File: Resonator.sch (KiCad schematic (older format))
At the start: 25 parts, among them SW1 SW_Push, U1 PCM3060, U5 STM32H750VBTx, Y1 25MHz

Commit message: Chanced regulators and oscillator work.
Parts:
- added R2: 10k, Resistor_SMD:R_0603_1608Metric, symbol Device:R
- added R3: 470, Resistor_SMD:R_0603_1608Metric, symbol Device:R
- C11: renamed from C43; footprint Capacitor_SMD:C_0603_1608Metric -> Capacitor_SMD:C_0402_1005Metric
- C12: renamed from C44; footprint Capacitor_SMD:C_0603_1608Metric -> Capacitor_SMD:C_0402_1005Metric
- C13: renamed from C45; footprint Capacitor_SMD:C_0603_1608Metric -> Capacitor_SMD:C_0402_1005Metric
- C15: renamed from C47; footprint Capacitor_SMD:C_0603_1608Metric -> Capacitor_SMD:C_0402_1005Metric
- C16: renamed from C1; footprint Capacitor_SMD:C_0603_1608Metric -> Capacitor_SMD:C_0402_1005Metric
- C17: renamed from C2; footprint Capacitor_SMD:C_0603_1608Metric -> Capacitor_SMD:C_0402_1005Metric
- C18: renamed from C3; footprint Capacitor_SMD:C_0603_1608Metric -> Capacitor_SMD:C_0402_1005Metric
- C2: renamed from C34; footprint Capacitor_SMD:C_0603_1608Metric -> Capacitor_SMD:C_0402_1005Metric
- C3: renamed from C35; footprint Capacitor_SMD:C_0603_1608Metric -> Capacitor_SMD:C_0402_1005Metric
- C4: renamed from C36; footprint Capacitor_SMD:C_0603_1608Metric -> Capacitor_SMD:C_0402_1005Metric
- C5: renamed from C37; footprint Capacitor_SMD:C_0603_1608Metric -> Capacitor_SMD:C_0402_1005Metric
- C6: renamed from C41; value 3p9 -> 22p; footprint Capacitor_SMD:C_0603_1608Metric -> Capacitor_SMD:C_0402_1005Metric
- C7: renamed from C42; value 3p9 -> 22p; footprint Capacitor_SMD:C_0603_1608Metric -> Capacitor_SMD:C_0402_1005Metric
- C9: renamed from C39; footprint Capacitor_SMD:C_0603_1608Metric -> Capacitor_SMD:C_0402_1005Metric
- R1: renamed from R23; value 10k -> UNPOPULATED
- SW1: footprint (none) -> Button_Switch_THT:SW_PUSH_6mm
- Y1: value 25MHz -> ABM8G-25.000MHZ-18-D2Y-T; footprint (none) -> Crystal:Crystal_SMD_Abracon_ABM8G-4Pin_3.2x2.5mm
- renumbered C33 to C1, C40 to C10, C46 to C14, C4 to C19, C38 to C8, R1 to R4, U5 to U1, U1 to U2
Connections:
- net +3V3: now also R1.2
- net GND: now also R2.1
- net at C7.1, Y1.3: now also R3.2; no longer U1.13 (PH1)
- net at R1.1, U1.94 (BOOT0): now also R2.2
- new net: R3.1, U1.13 (PH1)
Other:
- moved on the sheet: C6, C7, R1, Y1

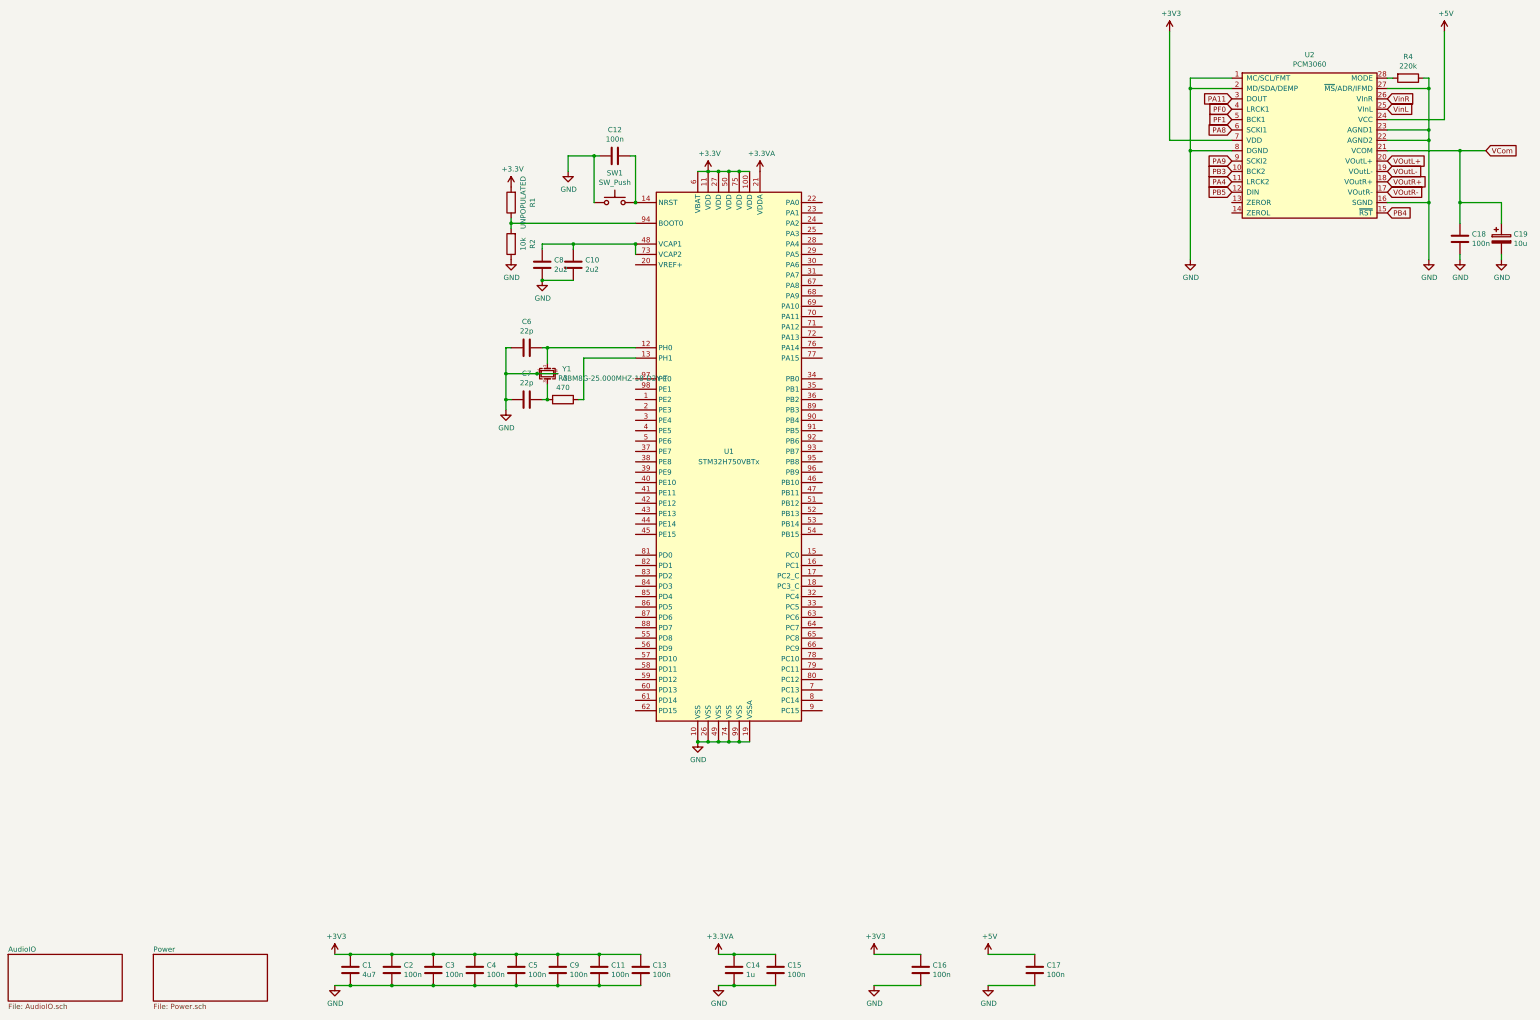
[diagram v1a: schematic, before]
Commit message: Added UI components.
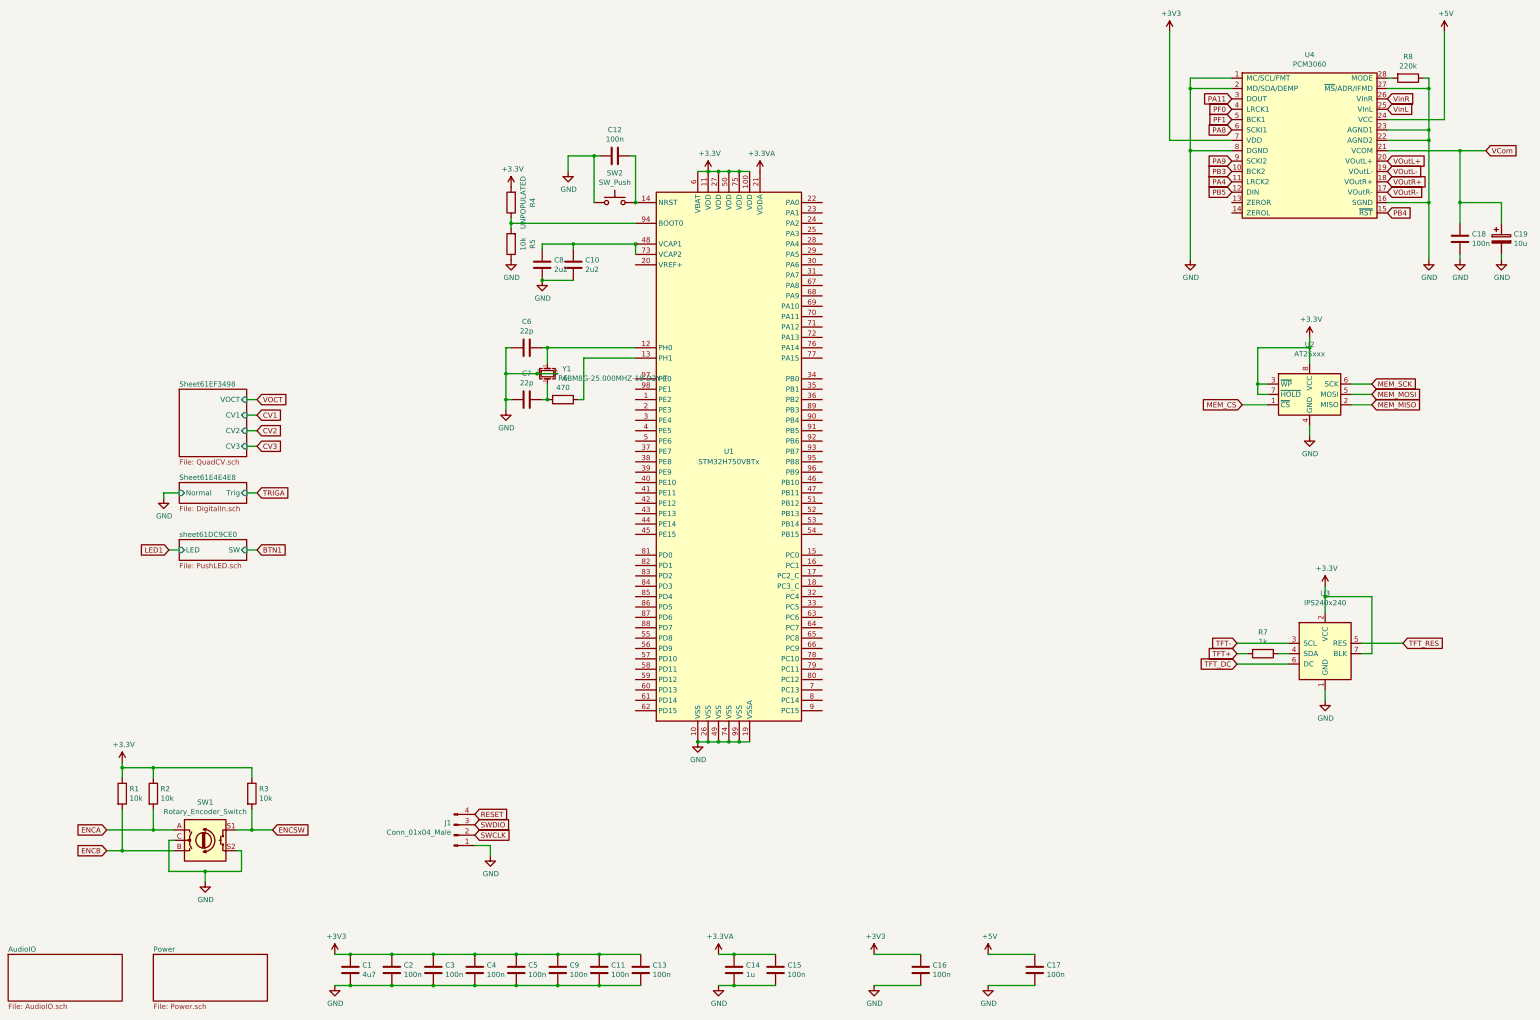
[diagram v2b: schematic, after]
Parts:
- added J1: Conn_01x04_Male, Connector_PinHeader_2.54mm:PinHeader_1x04_P2.54mm_Vertical, symbol Connector:Conn_01x04_Male
- added R1, R2, R3: 10k, Resistor_SMD:R_0603_1608Metric, symbol Device:R
- added R7: 1k, Resistor_SMD:R_0603_1608Metric, symbol Device:R
- added SW1: Rotary_Encoder_Switch, Rotary_Encoder:RotaryEncoder_Alps_EC11E-Switch_Vertical_H20mm, symbol Device:Rotary_Encoder_Switch
- added U2: AT25xxx, Package_SO:TSSOP-8_4.4x3mm_P0.65mm, symbol Memory_EEPROM:AT25xxx
- added U3: IPS240x240, symbol IPS240x240:IPS240x240
- renumbered R1 to R4, R2 to R5, R3 to R6, R4 to R8, SW1 to SW2, U2 to U4
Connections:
- net +3V3: now also R1.1, R2.1, R3.1, U2.3 (~WP), U2.7 (~HOLD), U2.8 (VCC), U3.2 (VCC), U3.7 (BLK)
- net GND: now also J1.1 (Pin_1), SW1.C, SW1.S2, U2.4 (GND), U3.1 (GND)
- new net: R7.1, U3.4 (SDA)
- new net ENCA: R2.2, SW1.A
- new net ENCB: R1.2, SW1.B
- new net ENCSW: R3.2, SW1.S1
- new net MEM_CS: U2.1 (~CS)
- new net MEM_MISO: U2.2 (MISO)
- new net MEM_MOSI: U2.5 (MOSI)
- new net MEM_SCK: U2.6 (SCK)
- new net RESET: J1.4 (Pin_4)
- new net SWCLK: J1.2 (Pin_2)
- new net SWDIO: J1.3 (Pin_3)
- new net TFT+: R7.2
- new net TFT-: U3.3 (SCL)
- new net TFT_DC: U3.6 (DC)
- new net TFT_RES: U3.5 (RES)

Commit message: Moved codec to audio module.
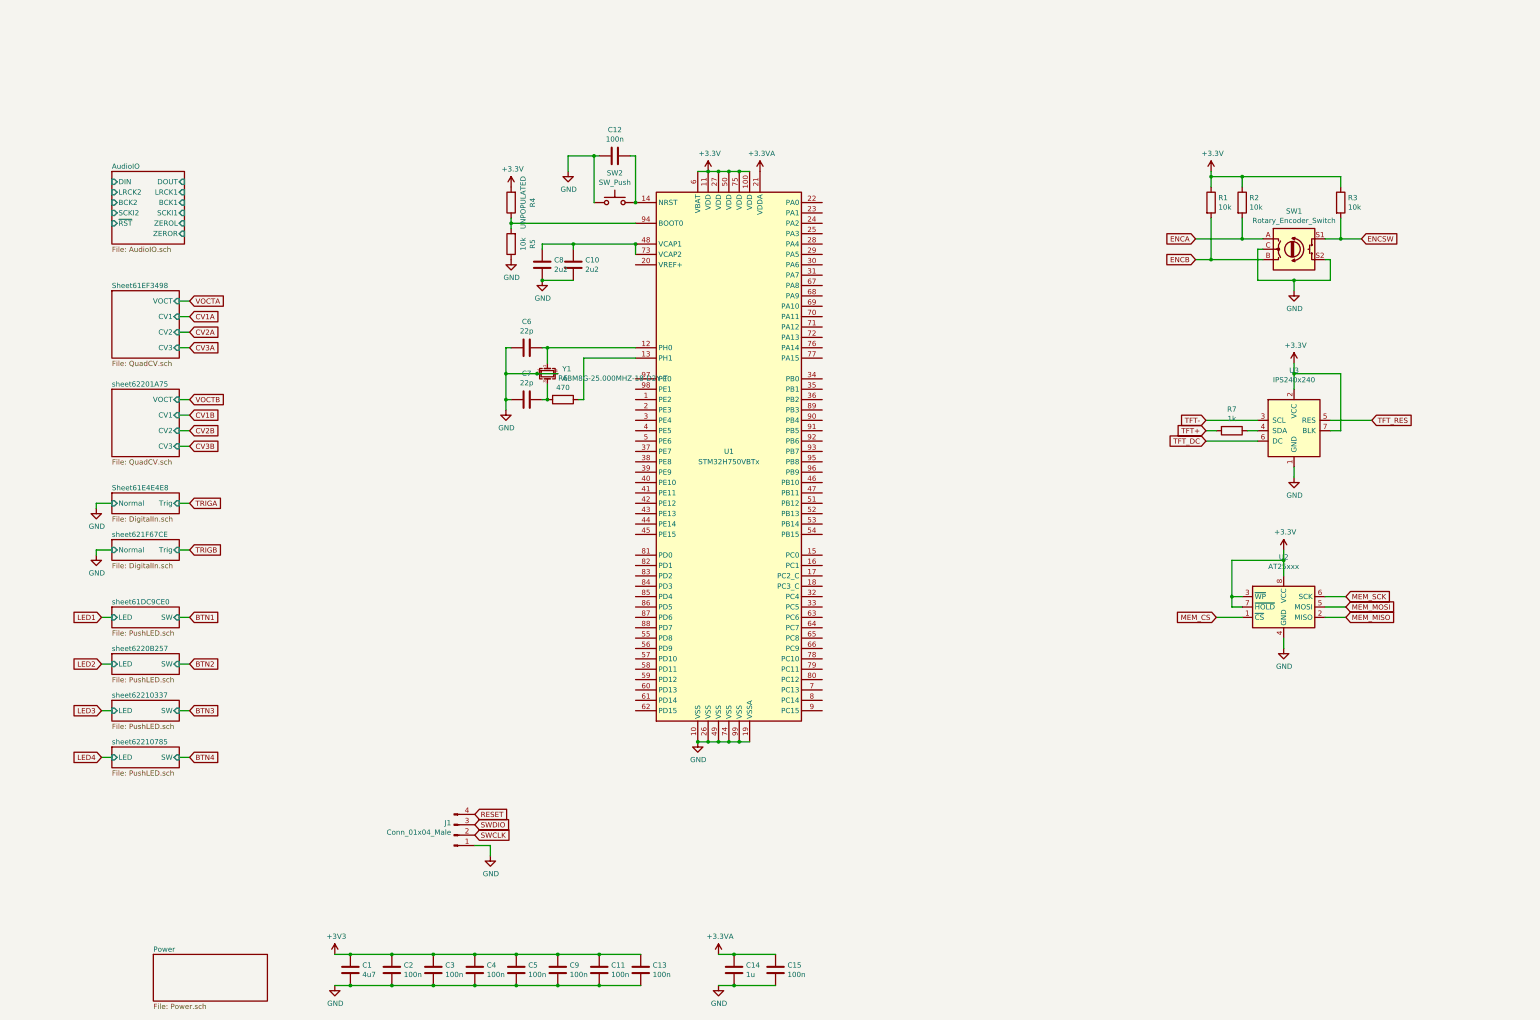
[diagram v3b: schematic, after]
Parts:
- removed C16, C17, C18: 100n, Capacitor_SMD:C_0402_1005Metric, symbol Device:C
- removed C19: 10u, Capacitor_SMD:C_0603_1608Metric, symbol Device:CP
- removed R8: 220k, Resistor_SMD:R_0603_1608Metric, symbol Device:R
- removed U4: PCM3060, Package_SO:TSSOP-28_4.4x9.7mm_P0.65mm, symbol PCM3060:PCM3060
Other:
- moved on the sheet: R1, R2, R3, R7, SW1, U2, U3
